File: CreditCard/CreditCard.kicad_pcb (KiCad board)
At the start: 2 copper layers, 50.8 x 88.9 mm, 86 parts, among them J1 2060-1452/998-404, J2 LCD, J3 12402012E212A, SW1 2425754-1, SW2 2425754-1, SW3 2425754-1, U1 BQ24230RGTR, U10 PAM8403DR, U11 SPKM.36.8.B, U2 MCP1603T-330I/OS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

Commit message: Alice grosse avancée
et oui!
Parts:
- 3VTP1, FID1, FID2, FID3, FID4, FID5, FID6, GNDTP1, TP1: moved to B.Cu
- moved 3VTP1 170.9 mm to (89.1, 66.8), turned to 180 degrees
- moved GNDTP1 170.9 mm to (89.1, 70.3), turned to 180 degrees
- moved TP1 170.9 mm to (89.1, 73.9), turned to 180 degrees
- moved FID1 164.4 mm to (85.8, 66.5), turned to 180 degrees
- moved FID2 164.4 mm to (85.8, 69.6), turned to 180 degrees
- moved FID3 158.3 mm to (82.8, 66.5), turned to 180 degrees
- moved FID4 158.3 mm to (82.8, 69.6), turned to 180 degrees
- moved FID5 152.3 mm to (79.7, 66.5), turned to 180 degrees
- moved FID6 152.3 mm to (79.7, 69.6), turned to 180 degrees
- moved F4 2.93 mm to (148.4, 64.3)
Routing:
- net GND: track 36.6 -> 109.5 mm, vias 1 -> 51
- net GPIO3: track 3.25 -> 60.8 mm, vias 0 -> 2
- net GPIO2: track 3.47 -> 59.3 mm, vias 0 -> 2
- net GPIO4: track 3.43 -> 58.8 mm
- net GPIO7: track 10.1 -> 63.8 mm, vias 0 -> 1
- net GPIO5: track 10.1 -> 61.7 mm, vias 0 -> 1
- net GPIO6: track 10.1 -> 61.4 mm, vias 0 -> 1
- net AudioR: track 0.00 -> 49.3 mm, vias 0 -> 2
- net LCD_D/C: track 0.00 -> 38.4 mm, vias 0 -> 2
- net SCK: track 0.00 -> 35.6 mm, vias 0 -> 2
- net LCD_RESET: track 0.00 -> 33.1 mm
- net IO_CHG: track 3.98 -> 36.1 mm, vias 0 -> 2
- net AudioL: track 0.00 -> 31.6 mm, vias 0 -> 2
- net MOSI: track 0.00 -> 30.5 mm, vias 0 -> 2
- net MISO: track 0.00 -> 28.2 mm, vias 0 -> 2
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- added copper zone on In2.Cu, net 3V3
- added copper zone on B.Cu, net GND
- added copper zone on In1.Cu, net GND
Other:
- copper layers 2 -> 4

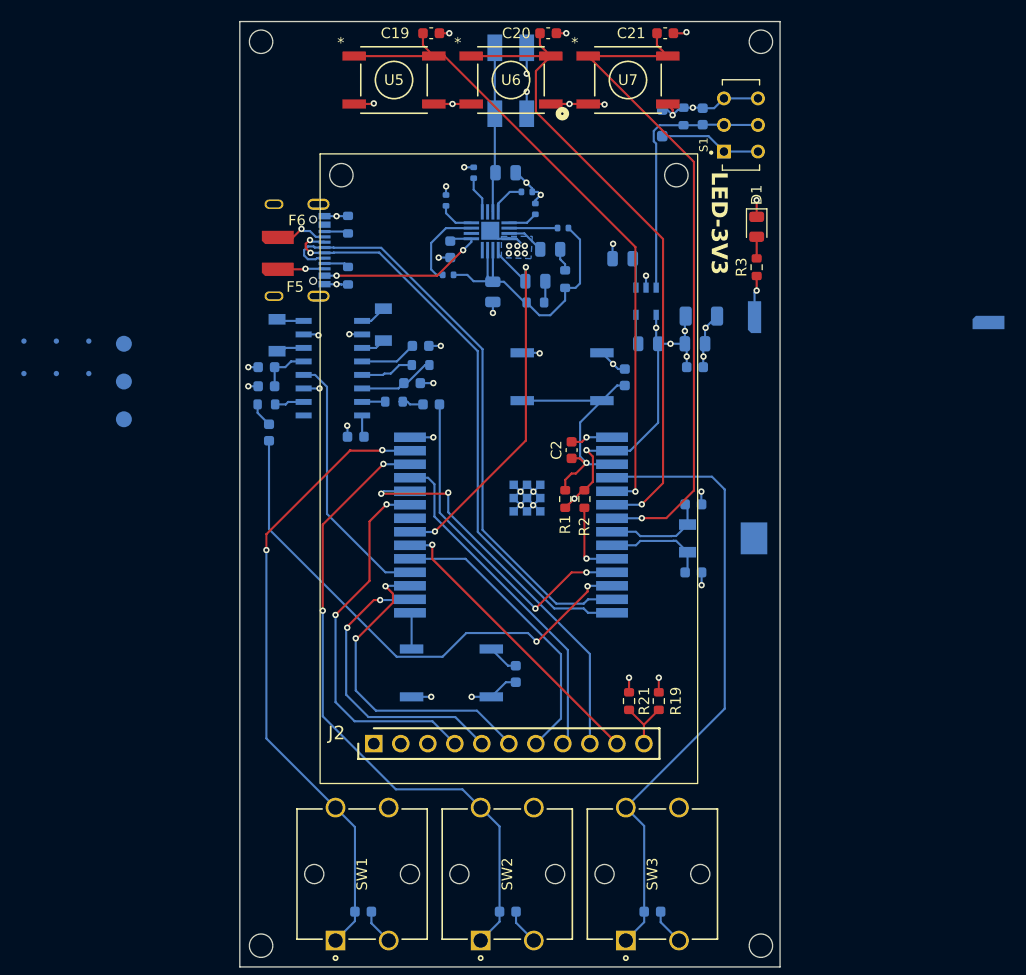
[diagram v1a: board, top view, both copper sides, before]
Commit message: gerber crée
pcb terminer
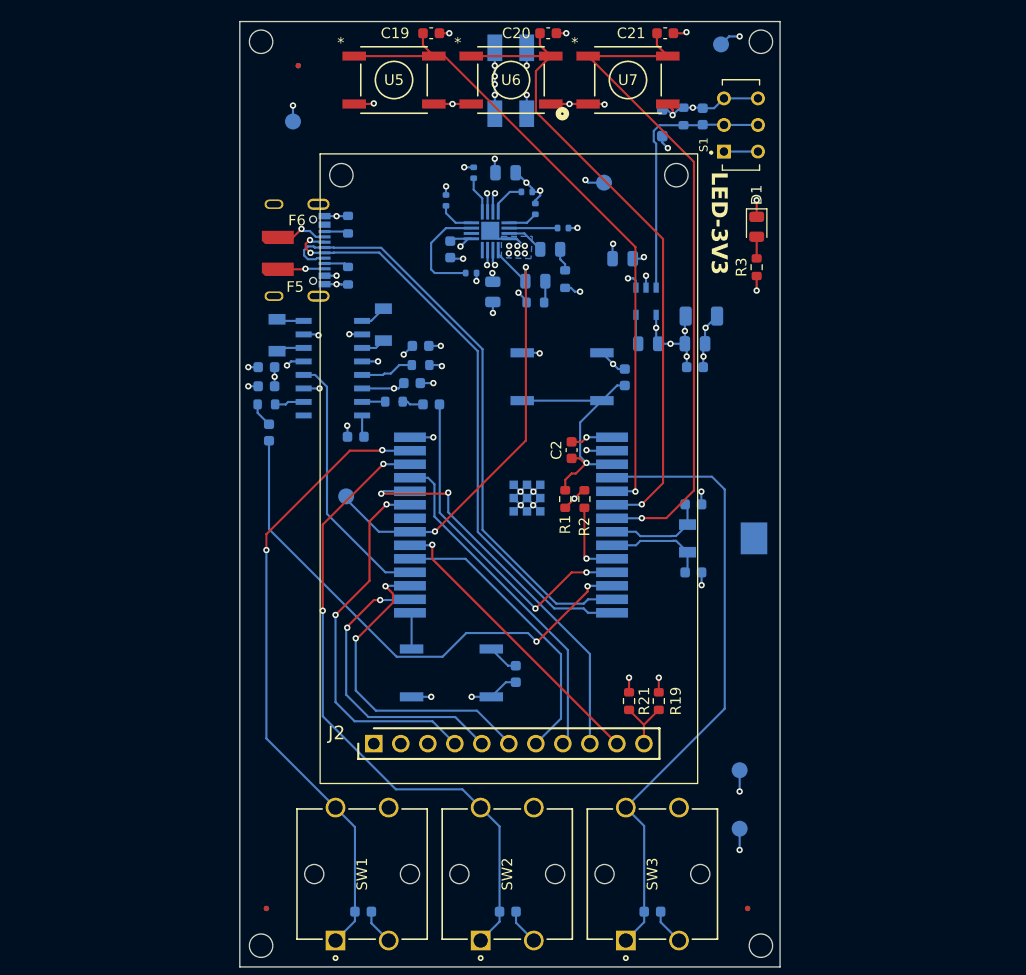
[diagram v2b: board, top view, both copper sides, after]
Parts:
- removed F3, F4: ~, Library:GOLD_FINGERS
- removed TP1: TestPoint, TestPoint:TestPoint_Pad_D1.5mm
- added IOCHG_TP1: TP, TestPoint:TestPoint_Pad_D1.5mm, B.Cu at (110.0, 81.2)
- added Vbat_TP1: TP, TestPoint:TestPoint_Pad_D1.5mm, B.Cu at (145.2, 38.6)
- added Vbus_TP1: TP, TestPoint:TestPoint_Pad_D1.5mm, B.Cu at (105.0, 45.9)
- added Vsys_TP1: TP, TestPoint:TestPoint_Pad_D1.5mm, B.Cu at (134.2, 51.6)
- FID1, FID4, FID5: moved to F.Cu
- moved FID3 84.1 mm to (147.8, 119.9)
- moved FID4 82.2 mm to (147.8, 119.9)
- moved GND_TP1 71.6 mm to (147.0, 112.4)
- moved 3V3_TP1 70.4 mm to (147.0, 106.9), turned to 0 degrees
- moved FID1 55.9 mm to (102.5, 119.9), turned to 0 degrees
- moved FID2 53.0 mm to (102.5, 119.9)
- moved FID6 38.8 mm to (105.5, 40.6)
- moved FID5 36.6 mm to (105.5, 40.6)
- moved R23 2.17 mm to (121.8, 60.1)
- renumbered 3VTP1 to 3V3_TP1, GNDTP1 to GND_TP1
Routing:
- net 3V3: track 55.7 -> 32.3 mm, vias 8 -> 15
- net Vsys: track 40.2 -> 18.3 mm, vias 0 -> 11
- net Vbus: track 17.5 -> 6.04 mm, vias 2 -> 3
- net IO_CHG: track 36.1 -> 43.4 mm
- net Vbat: track 15.8 -> 13.7 mm, vias 0 -> 8
- net /PWR/TD_CHR: track 8.15 -> 10.2 mm
- net GND: track 109.5 -> 110.8 mm, vias 51 -> 52
- added copper zone on In2.Cu, net Vbat
- added copper zone on In2.Cu, net Vbus
- added copper zone on In2.Cu, net Vsys

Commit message: petite retouche et bom complet
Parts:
- removed C24: 470uf, Capacitor_SMD:C_0603_1608Metric
- added C27: 0.1uF, Capacitor_SMD:C_0603_1608Metric, F.Cu at (110.5, 68.4)
- added C28: 0.1uF, Capacitor_SMD:C_0603_1608Metric, F.Cu at (106.8, 66.7)
- added C29: 0.1uF, Capacitor_SMD:C_0603_1608Metric, F.Cu at (110.5, 70.7)
- added C30: 0.1uF, Capacitor_SMD:C_0603_1608Metric, F.Cu at (110.5, 66.7)
- added C31: 0.1uF, Capacitor_SMD:C_0603_1608Metric, F.Cu at (111.8, 73.2)
- added C32: 0.1uF, Capacitor_SMD:C_0603_1608Metric, F.Cu at (102.8, 66.7)
- added C33: 0.1uF, Capacitor_SMD:C_0603_1608Metric, F.Cu at (102.8, 68.4)
- added C34: 0.1uF, Capacitor_SMD:C_0603_1608Metric, F.Cu at (106.8, 68.4)
- added C35: 0.1uF, Capacitor_SMD:C_0603_1608Metric, F.Cu at (114.5, 69.9)
- added C36: 0.1uF, Capacitor_SMD:C_0603_1608Metric, F.Cu at (104.8, 70.9)
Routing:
- net 3V3: track 32.3 -> 48.7 mm
- net GND: track 110.8 -> 123.4 mm, vias 52 -> 56
